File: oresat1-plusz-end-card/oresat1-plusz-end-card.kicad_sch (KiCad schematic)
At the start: 35 parts, among them J1 J-SAMTEC-TFM-120-01-L-D-RA, J2 M55-7101242R, J3 M55-7101242R, J4 M55-7101242R, J5 M55-7101242R, J6 U.FL-R-SMT-1

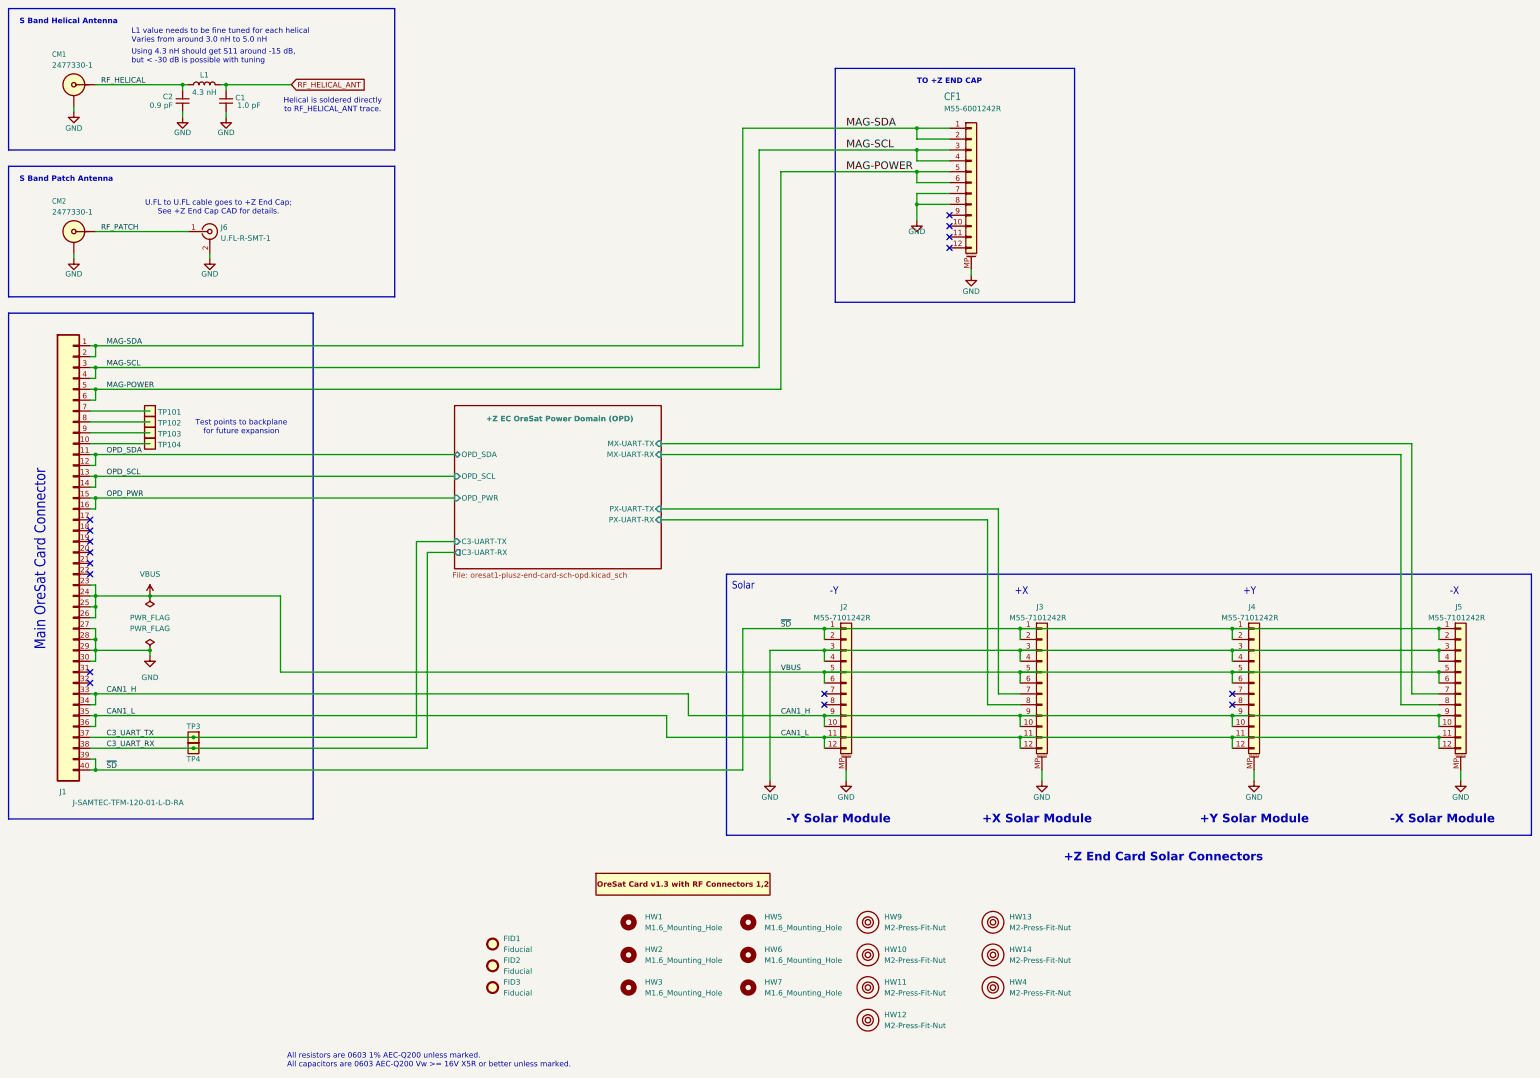
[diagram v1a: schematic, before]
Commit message: v1.2 for fab (hopefully)
Re-Added UART switches for PY and MY (why were they removed?) and cleaned up schematic and routing a bit.
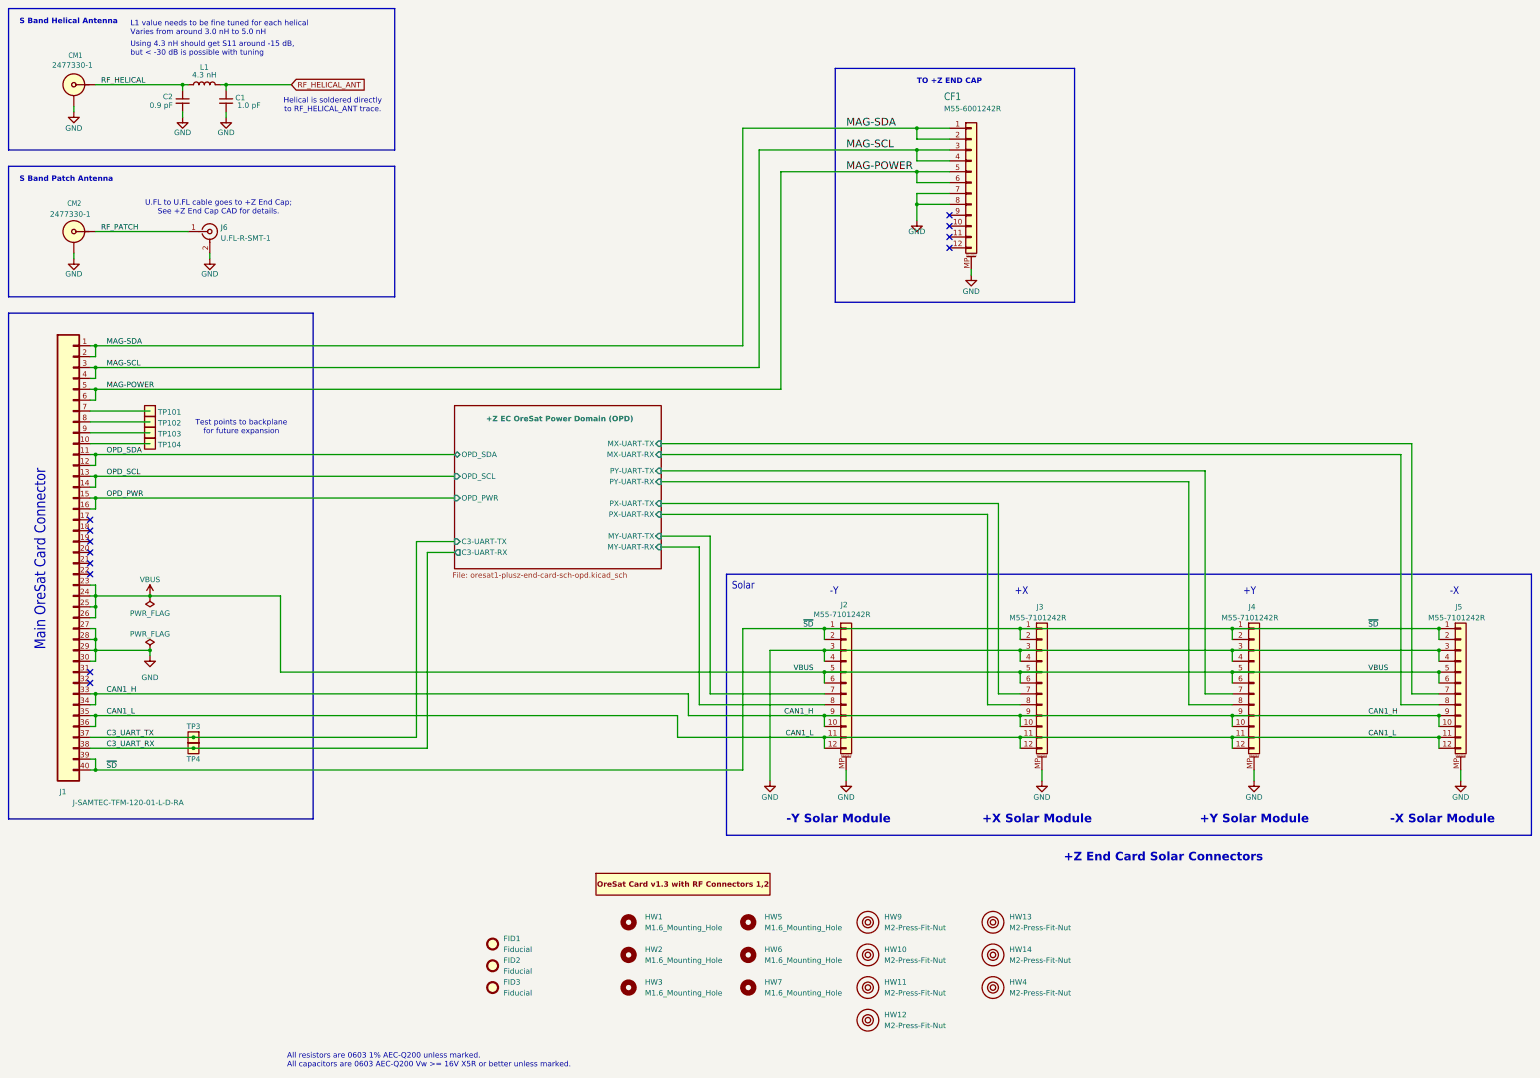
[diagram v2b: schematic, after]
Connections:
- net +Z EC OreSat Power Domain (OPD)/MY-UART-TX: now reaches J2.7 (Pin_7)
- net +Z EC OreSat Power Domain (OPD)/MY-UART-RX: now reaches J2.8 (Pin_8)
- net +Z EC OreSat Power Domain (OPD)/PY-UART-TX: now reaches J4.7 (Pin_7)
- net +Z EC OreSat Power Domain (OPD)/PY-UART-RX: now reaches J4.8 (Pin_8)
- no-connect marks 16 -> 12
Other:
- sheet +Z EC OreSat Power Domain (OPD) ports: added MY-UART-RX, MY-UART-TX, PY-UART-RX, PY-UART-TX; removed none
